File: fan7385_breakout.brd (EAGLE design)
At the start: 28.6 x 15.2 mm, 15 parts

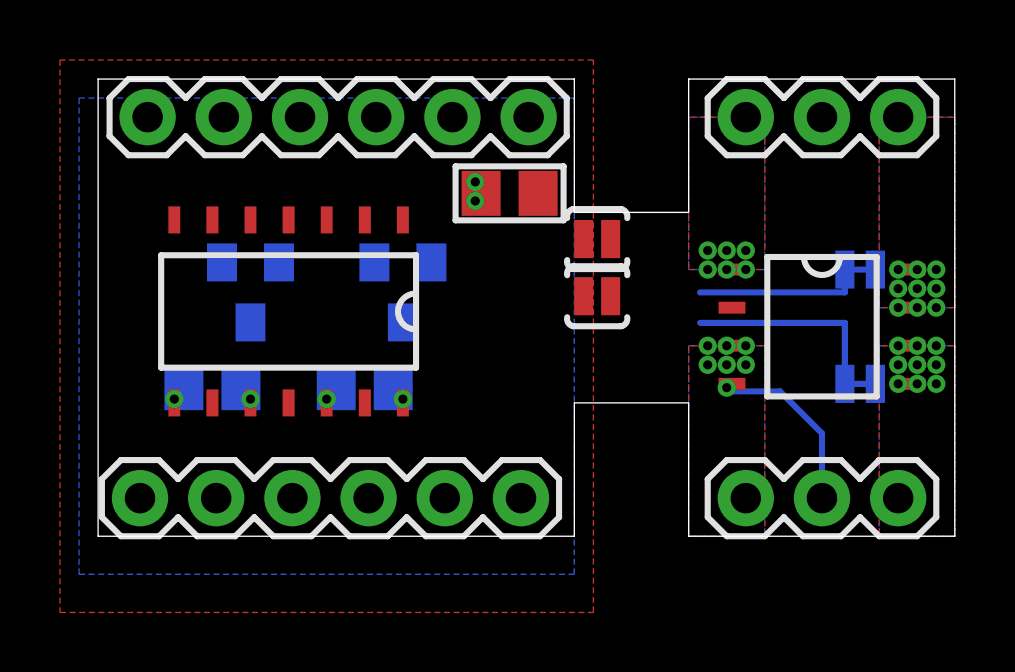
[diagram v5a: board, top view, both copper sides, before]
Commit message: labels and optimizing size
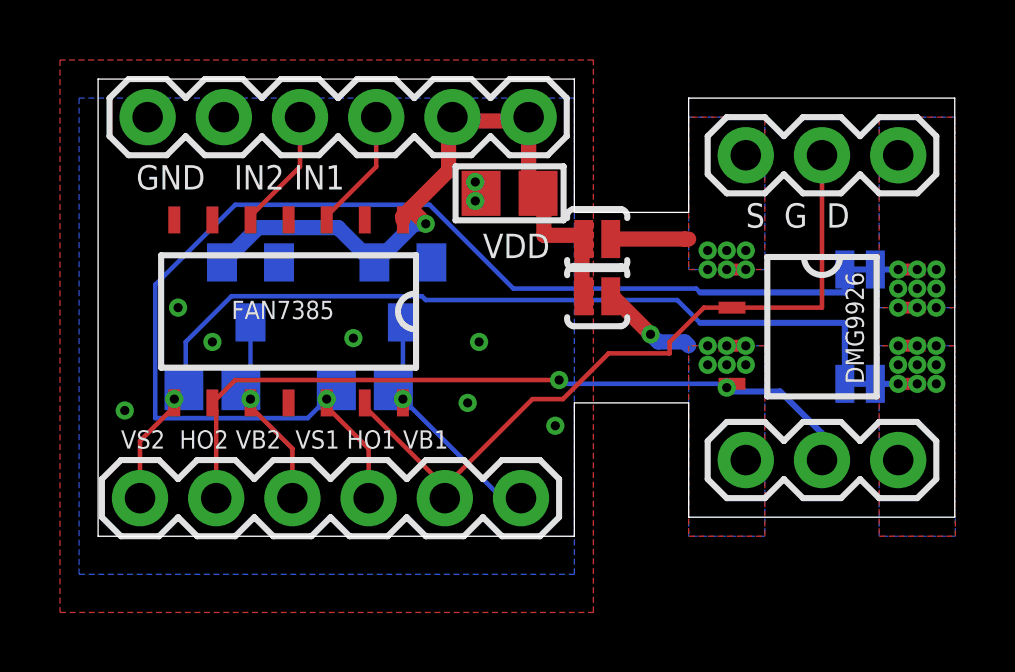
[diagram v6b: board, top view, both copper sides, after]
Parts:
- moved JP4 1.27 mm to (21.6, 12.7)
- moved JP3 1.27 mm to (21.6, 2.54)
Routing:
- net VS1: track 5.59 -> 41.1 mm
- net HO1/G1: track 0.00 -> 25.0 mm
- net VS2: track 6.86 -> 31.1 mm
- net VDD: track 0.00 -> 23.3 mm, vias 0 -> 1
- net HO2/G2: track 6.19 -> 25.7 mm, vias 1 -> 2
- net VB1: track 0.00 -> 8.53 mm
- net VB2: track 0.00 -> 7.10 mm
- net IN2: track 0.00 -> 4.11 mm
- net IN1: track 0.00 -> 4.11 mm
- net S2: track 0.00 -> 3.28 mm, vias 6 -> 7
- net S1: track 0.00 -> 2.60 mm
- net D2: track 0.00 -> 0.76 mm
- net D1: track 0.00 -> 0.76 mm
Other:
- outline, holes or cut-outs redrawn
- board text added: "DMG9926"
- board text added: "FAN7385"
- board text added: "GND IN2 IN1"
- board text added: "S G D"
- board text added: "VDD"
- board text added: "VS2 HO2 VB2 VS1 HO1 VB1"

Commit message: adjusted mosfet position to allow for pin labels
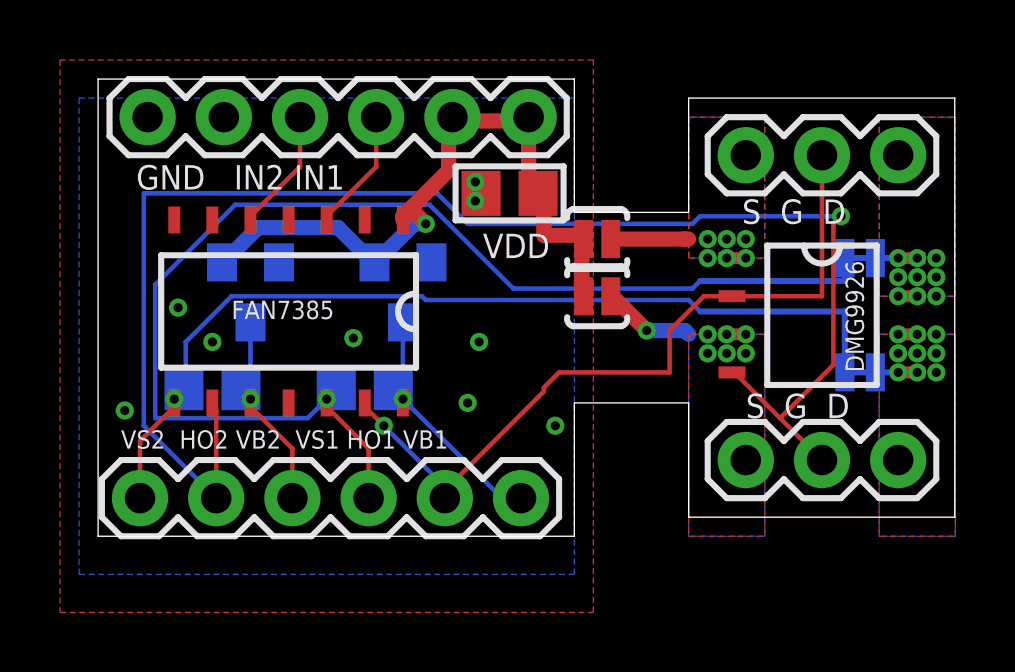
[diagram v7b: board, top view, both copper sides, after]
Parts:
- moved SJ3 0.38 mm to (25.4, 9.27)
- moved SJ4 0.38 mm to (25.4, 5.46)
- moved FET 0.38 mm to (24.1, 7.37)
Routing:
- net HO2/G2: track 25.7 -> 49.9 mm, vias 2 -> 1
- net HO1/G1: track 25.0 -> 25.4 mm, vias 0 -> 1

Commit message: actually if these are to be used together the pin aligment must match...
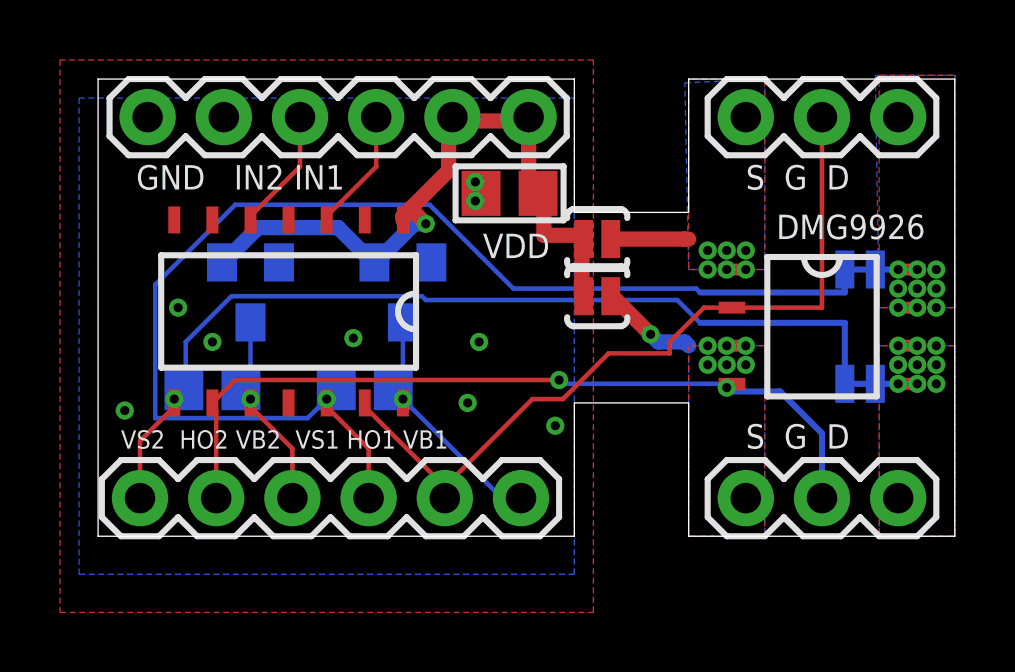
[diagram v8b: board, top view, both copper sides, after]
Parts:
- moved JP4 1.27 mm to (21.6, 14.0)
- moved JP3 1.27 mm to (21.6, 1.27)
- moved SJ3 0.38 mm to (25.4, 8.89)
- moved SJ4 0.38 mm to (25.4, 5.08)
- moved FET 0.38 mm to (24.1, 6.99)
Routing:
- net HO2/G2: track 49.9 -> 27.0 mm, vias 1 -> 2
- net HO1/G1: track 25.4 -> 26.3 mm, vias 1 -> 0
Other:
- outline, holes or cut-outs redrawn
- board text removed: "FAN7385"
